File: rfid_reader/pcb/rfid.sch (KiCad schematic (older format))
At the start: 25 parts, among them IC1 ATMEGA8-P, P1 CONN_2, P2 CONN_4, P3 CONN_2, Q1 BS107, Q2 BC547, U1 LM358, X1 8MHz

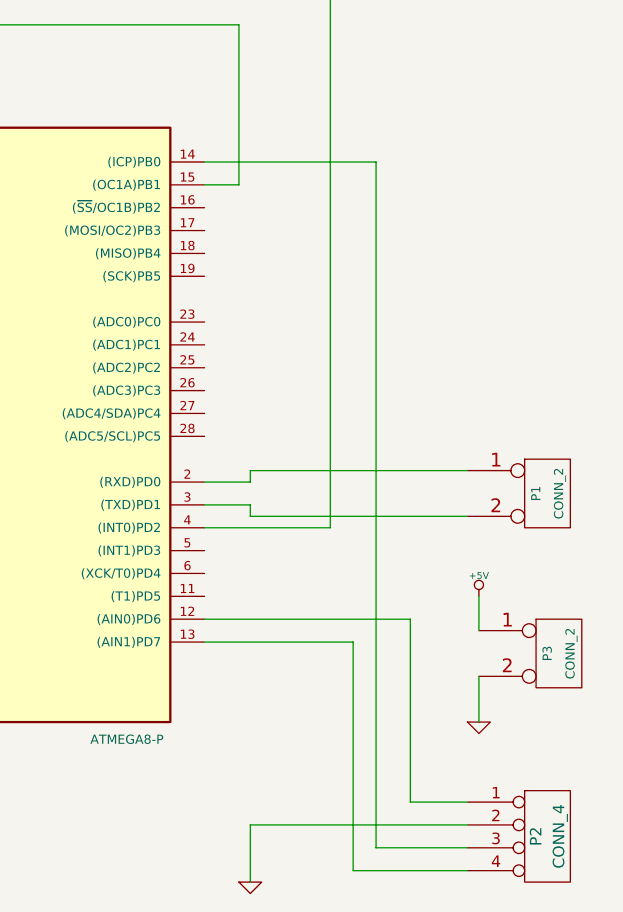
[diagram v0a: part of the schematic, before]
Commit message: Added I2C to PSB
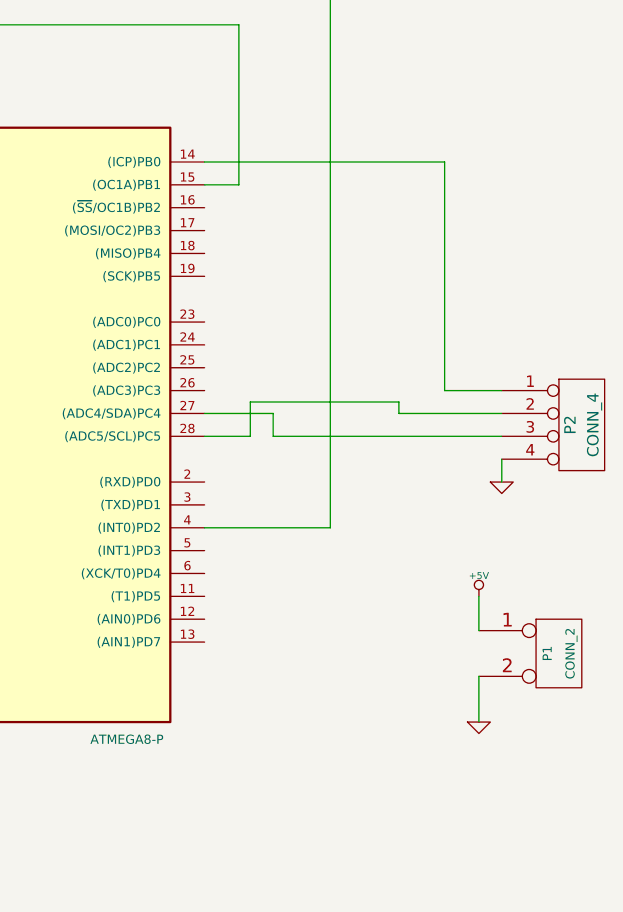
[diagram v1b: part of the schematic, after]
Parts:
- removed P1: CONN_2, symbol CONN_2
- renumbered P3 to P1
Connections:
- net GND: now also P2.4 (P4); no longer P2.2 (P2)
- net at IC1.12 ((AIN0)PD6): no longer P2.1 (P1)
- net at IC1.13 ((AIN1)PD7): no longer P2.4 (P4)
- net at IC1.14 ((ICP)PB0): now also P2.1 (P1); no longer P2.3 (P3)
- net at IC1.27 ((ADC4/SDA)PC4): now also P2.3 (P3)
- net at IC1.28 ((ADC5/SCL)PC5): now also P2.2 (P2)
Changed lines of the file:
@@
 LIBS:contrib
 LIBS:valves
+LIBS:rfid-cache
 EELAYER 27 0
 EELAYER END
@@
 Sheet 1 1
 Title ""
-Date "13 apr 2014"
+Date "21 apr 2014"
 Rev ""
 Comp ""
@@
 $Comp
 L CONN_2 P1
-U 1 1 534AE1FA
-P 8000 5300
-F 0 "P1" V 7950 5300 40  0000 C CNN
-F 1 "CONN_2" V 8050 5300 40  0000 C CNN
-F 2 "" H 8000 5300 60  0000 C CNN
-F 3 "" H 8000 5300 60  0000 C CNN
-	1    8000 5300
-	1    0    0    -1
-$EndComp
-Wire Wire Line
-	6500 5350 6700 5350
-Wire Wire Line
-	6700 5350 6700 5400
-Wire Wire Line
-	6700 5400 7650 5400
-Wire Wire Line
-	6500 5250 6700 5250
-Wire Wire Line
-	6700 5250 6700 5200
-Wire Wire Line
-	6700 5200 7650 5200
-$Comp
-L CONN_2 P3
 U 1 1 534AE35B
 P 8050 6000
-F 0 "P3" V 8000 6000 40  0000 C CNN
+F 0 "P1" V 8000 6000 40  0000 C CNN
 F 1 "CONN_2" V 8100 6000 40  0000 C CNN
 F 2 "" H 8050 6000 60  0000 C CNN
@@
 $EndComp
 $Comp
-L +5V #PWR18
+L +5V #PWR17
 U 1 1 534AE361
 P 7700 5750
-F 0 "#PWR18" H 7700 5840 20  0001 C CNN
+F 0 "#PWR17" H 7700 5840 20  0001 C CNN
 F 1 "+5V" H 7700 5840 30  0000 C CNN
 F 2 "" H 7700 5750 60  0000 C CNN
@@
 $EndComp
 $Comp
-L GND #PWR19
+L GND #PWR18
 U 1 1 534AE367
 P 7700 6300
-F 0 "#PWR19" H 7700 6300 30  0001 C CNN
+F 0 "#PWR18" H 7700 6300 30  0001 C CNN
 F 1 "GND" H 7700 6230 30  0001 C CNN
 F 2 "" H 7700 6300 60  0000 C CNN
@@
 Wire Wire Line
 	7700 6100 7700 6300
+Wire Wire Line
+	6500 3850 7550 3850
+Wire Wire Line
+	7550 3850 7550 4850
+Wire Wire Line
+	7550 4850 7800 4850
+Wire Wire Line
+	6800 5050 7800 5050
+Wire Wire Line
+	6800 5050 6800 4950
+Wire Wire Line
+	6800 4950 6500 4950
 $Comp
 L CONN_4 P2
-U 1 1 534AE5AF
-P 8000 6800
-F 0 "P2" V 7950 6800 50  0000 C CNN
-F 1 "CONN_4" V 8050 6800 50  0000 C CNN
-F 2 "" H 8000 6800 60  0000 C CNN
-F 3 "" H 8000 6800 60  0000 C CNN
-	1    8000 6800
-	1    0    0    -1
-$EndComp
-Wire Wire Line
-	6500 5850 7400 5850
-Wire Wire Line
-	7400 5850 7400 6650
-Wire Wire Line
-	7400 6650 7650 6650
-Wire Wire Line
-	6500 3850 7250 3850
-Wire Wire Line
-	7250 3850 7250 6850
-Wire Wire Line
-	7250 6850 7650 6850
-Wire Wire Line
-	6500 5950 7150 5950
-Wire Wire Line
-	7150 5950 7150 6950
-Wire Wire Line
-	7150 6950 7650 6950
-$Comp
-L GND #PWR17
-U 1 1 534AE6E0
-P 6700 7000
-F 0 "#PWR17" H 6700 7000 30  0001 C CNN
-F 1 "GND" H 6700 6930 30  0001 C CNN
-F 2 "" H 6700 7000 60  0000 C CNN
-F 3 "" H 6700 7000 60  0000 C CNN
-	1    6700 7000
-	1    0    0    -1
-$EndComp
-Wire Wire Line
-	7650 6750 6700 6750
-Wire Wire Line
-	6700 6750 6700 7000
+U 1 1 53555009
+P 8150 5000
+F 0 "P2" V 8100 5000 50  0000 C CNN
+F 1 "CONN_4" V 8200 5000 50  0000 C CNN
+F 2 "" H 8150 5000 60  0000 C CNN
+F 3 "" H 8150 5000 60  0000 C CNN
+	1    8150 5000
+	1    0    0    -1
+$EndComp
+Wire Wire Line
+	6500 5050 6700 5050
+Wire Wire Line
+	6700 5050 6700 4900
+Wire Wire Line
+	6700 4900 7350 4900
+Wire Wire Line
+	7350 4900 7350 4950
+Wire Wire Line
+	7350 4950 7800 4950
+$Comp
+L GND #PWR19
+U 1 1 53555134
+P 7800 5250
+F 0 "#PWR19" H 7800 5250 30  0001 C CNN
+F 1 "GND" H 7800 5180 30  0001 C CNN
+F 2 "" H 7800 5250 60  0000 C CNN
+F 3 "" H 7800 5250 60  0000 C CNN
+	1    7800 5250
+	1    0    0    -1
+$EndComp
+Wire Wire Line
+	7800 5150 7800 5250
 $EndSCHEMATC
